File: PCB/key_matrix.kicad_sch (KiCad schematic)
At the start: 36 parts

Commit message: latest changes
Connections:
- net COL-3: now also MX116.1
- net COL-4: now also MX117.1
- net COL-5: now also MX118.1
- net ROW-1: no longer D116.1 (K)
- net ROW-2: no longer D117.1 (K)
- net ROW-3: no longer D118.1 (K)
- removed net COL-6: MX116.1, MX117.1, MX118.1
- new net ROW-4: D116.1 (K), D117.1 (K), D118.1 (K)
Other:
- moved on the sheet: D101, D102, D103, D104, D105, D106, D107, D108, D109, D110, D111, D112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

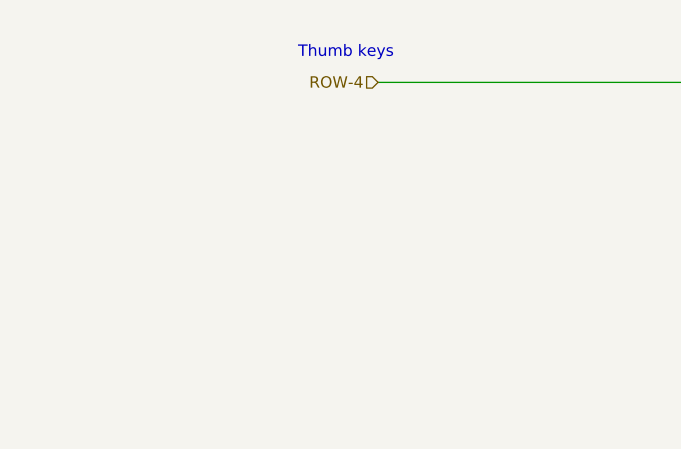
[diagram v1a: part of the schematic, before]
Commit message: Add mounting holes
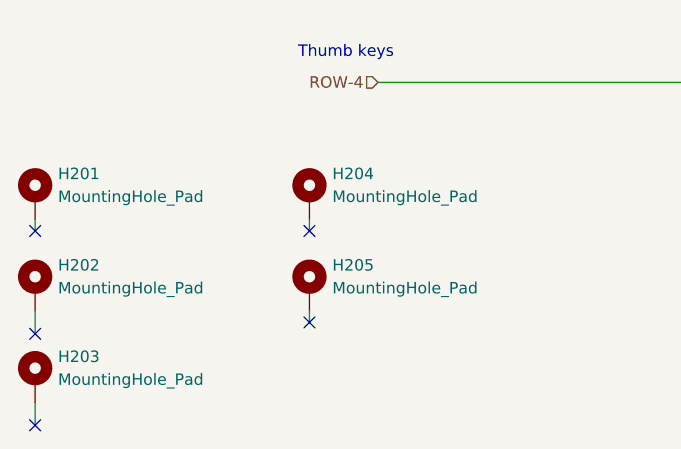
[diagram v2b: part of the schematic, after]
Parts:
- added H201, H202, H203, H204, H205: MountingHole_Pad, Footprints:M2_HOLE_v3, symbol Mechanical:MountingHole_Pad
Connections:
- no-connect marks 0 -> 5
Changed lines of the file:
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@@
   (junction (at 72.39 49.53) (diameter 0) (color 0 0 0 0)
   )
+  (no_connect (at 21.59 123.19))
+  (no_connect (at 21.59 133.35))
+  (no_connect (at 52.07 111.76))
+  (no_connect (at 52.07 121.92))
+  (no_connect (at 21.59 111.76))
   (wire (pts (xy 80.01 41.91) (xy 80.01 57.15))
     (stroke (width 0) (type default) (color 0 0 0 0))
@@
     (stroke (width 0) (type default) (color 0 0 0 0))
   )
+  (wire (pts (xy 52.07 110.49) (xy 52.07 111.76))
+    (stroke (width 0) (type default) (color 0 0 0 0))
+  )
   (wire (pts (xy 72.39 80.01) (xy 90.17 80.01))
     (stroke (width 0) (type default) (color 0 0 0 0))
   )
+  (wire (pts (xy 21.59 130.81) (xy 21.59 133.35))
+    (stroke (width 0) (type default) (color 0 0 0 0))
+  )
   (wire (pts (xy 125.73 95.25) (xy 143.51 95.25))
     (stroke (width 0) (type default) (color 0 0 0 0))
@@
     (stroke (width 0) (type default) (color 0 0 0 0))
   )
+  (wire (pts (xy 21.59 120.65) (xy 21.59 123.19))
+    (stroke (width 0) (type default) (color 0 0 0 0))
+  )
   (wire (pts (xy 97.79 33.02) (xy 97.79 41.91))
     (stroke (width 0) (type default) (color 0 0 0 0))
@@
     (stroke (width 0) (type default) (color 0 0 0 0))
   )
+  (wire (pts (xy 52.07 120.65) (xy 52.07 121.92))
+    (stroke (width 0) (type default) (color 0 0 0 0))
+  )
   (wire (pts (xy 115.57 72.39) (xy 115.57 87.63))
+    (stroke (width 0) (type default) (color 0 0 0 0))
+  )
+  (wire (pts (xy 21.59 111.76) (xy 21.59 110.49))
     (stroke (width 0) (type default) (color 0 0 0 0))
   )
@@
     (pin "2")
   )
+  (symbol (lib_id "Mechanical:MountingHole_Pad") (at 21.59 128.27 0) (unit 1)
+    (in_bom yes) (on_board yes) (fields_autoplaced)
+    (property "Reference" "H203" (id 0) (at 24.13 125.7299 0)
+      (effects (font (size 1.27 1.27)) (justify left))
+    )
+    (property "Value" "MountingHole_Pad" (id 1) (at 24.13 128.2699 0)
+      (effects (font (size 1.27 1.27)) (justify left))
+    )
+    (property "Footprint" "Footprints:M2_HOLE_v3" (id 2) (at 21.59 128.27 0)
+      (effects (font (size 1.27 1.27)) hide)
+    )
+    (property "Datasheet" "~" (id 3) (at 21.59 128.27 0)
+      (effects (font (size 1.27 1.27)) hide)
+    )
+    (pin "1")
+  )
   (symbol (lib_id "Switch:SW_Push") (at 102.87 87.63 0) (unit 1)
     (in_bom yes) (on_board yes)
@@
     (pin "2")
   )
+  (symbol (lib_id "Mechanical:MountingHole_Pad") (at 21.59 118.11 0) (unit 1)
+    (in_bom yes) (on_board yes) (fields_autoplaced)
+    (property "Reference" "H202" (id 0) (at 24.13 115.5699 0)
+      (effects (font (size 1.27 1.27)) (justify left))
+    )
+    (property "Value" "MountingHole_Pad" (id 1) (at 24.13 118.1099 0)
+      (effects (font (size 1.27 1.27)) (justify left))
+    )
+    (property "Footprint" "Footprints:M2_HOLE_v3" (id 2) (at 21.59 118.11 0)
+      (effects (font (size 1.27 1.27)) hide)
+    )
+    (property "Datasheet" "~" (id 3) (at 21.59 118.11 0)
+      (effects (font (size 1.27 1.27)) hide)
+    )
+    (pin "1")
+  )
   (symbol (lib_id "Diode:1N4148W") (at 125.73 60.96 270) (mirror x) (unit 1)
     (in_bom yes) (on_board yes)
@@
     (pin "2")
   )
+  (symbol (lib_id "Mechanical:MountingHole_Pad") (at 52.07 118.11 0) (unit 1)
+    (in_bom yes) (on_board yes) (fields_autoplaced)
+    (property "Reference" "H205" (id 0) (at 54.61 115.5699 0)
+      (effects (font (size 1.27 1.27)) (justify left))
+    )
+    (property "Value" "MountingHole_Pad" (id 1) (at 54.61 118.1099 0)
+      (effects (font (size 1.27 1.27)) (justify left))
+    )
+    (property "Footprint" "Footprints:M2_HOLE_v3" (id 2) (at 52.07 118.11 0)
+      (effects (font (size 1.27 1.27)) hide)
+    )
+    (property "Datasheet" "~" (id 3) (at 52.07 118.11 0)
+      (effects (font (size 1.27 1.27)) hide)
+    )
+    (pin "1")
+  )
   (symbol (lib_id "Diode:1N4148W") (at 90.17 76.2 90) (unit 1)
     (in_bom yes) (on_board yes)
@@
     (pin "2")
   )
+  (symbol (lib_id "Mechanical:MountingHole_Pad") (at 52.07 107.95 0) (unit 1)
+    (in_bom yes) (on_board yes) (fields_autoplaced)
+    (property "Reference" "H204" (id 0) (at 54.61 105.4099 0)
+      (effects (font (size 1.27 1.27)) (justify left))
+    )
+    (property "Value" "MountingHole_Pad" (id 1) (at 54.61 107.9499 0)
+      (effects (font (size 1.27 1.27)) (justify left))
+    )
+    (property "Footprint" "Footprints:M2_HOLE_v3" (id 2) (at 52.07 107.95 0)
+      (effects (font (size 1.27 1.27)) hide)
+    )
+    (property "Datasheet" "~" (id 3) (at 52.07 107.95 0)
+      (effects (font (size 1.27 1.27)) hide)
+    )
+    (pin "1")
+  )
   (symbol (lib_id "Diode:1N4148W") (at 107.95 60.96 270) (mirror x) (unit 1)
     (in_bom yes) (on_board yes)
@@
     (pin "2")
   )
+  (symbol (lib_id "Mechanical:MountingHole_Pad") (at 21.59 107.95 0) (unit 1)
+    (in_bom yes) (on_board yes) (fields_autoplaced)
+    (property "Reference" "H201" (id 0) (at 24.13 105.4099 0)
+      (effects (font (size 1.27 1.27)) (justify left))
+    )
+    (property "Value" "MountingHole_Pad" (id 1) (at 24.13 107.9499 0)
+      (effects (font (size 1.27 1.27)) (justify left))
+    )
+    (property "Footprint" "Footprints:M2_HOLE_v3" (id 2) (at 21.59 107.95 0)
+      (effects (font (size 1.27 1.27)) hide)
+    )
+    (property "Datasheet" "~" (id 3) (at 21.59 107.95 0)
+      (effects (font (size 1.27 1.27)) hide)
+    )
+    (pin "1")
+  )
   (symbol (lib_id "Diode:1N4148W") (at 72.39 76.2 270) (mirror x) (unit 1)

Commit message: Metric
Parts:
- renumbered H201 to H101, H202 to H102, H203 to H103, H204 to H104, H205 to H105
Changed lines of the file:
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@@
   (symbol (lib_id "Mechanical:MountingHole_Pad") (at 21.59 128.27 0) (unit 1)
     (in_bom yes) (on_board yes) (fields_autoplaced)
-    (property "Reference" "H203" (id 0) (at 24.13 125.7299 0)
+    (property "Reference" "H103" (id 0) (at 24.13 125.7299 0)
       (effects (font (size 1.27 1.27)) (justify left))
     )
@@
   (symbol (lib_id "Mechanical:MountingHole_Pad") (at 21.59 118.11 0) (unit 1)
     (in_bom yes) (on_board yes) (fields_autoplaced)
-    (property "Reference" "H202" (id 0) (at 24.13 115.5699 0)
+    (property "Reference" "H102" (id 0) (at 24.13 115.5699 0)
       (effects (font (size 1.27 1.27)) (justify left))
     )
@@
   (symbol (lib_id "Mechanical:MountingHole_Pad") (at 52.07 118.11 0) (unit 1)
     (in_bom yes) (on_board yes) (fields_autoplaced)
-    (property "Reference" "H205" (id 0) (at 54.61 115.5699 0)
+    (property "Reference" "H105" (id 0) (at 54.61 115.5699 0)
       (effects (font (size 1.27 1.27)) (justify left))
     )
@@
   (symbol (lib_id "Mechanical:MountingHole_Pad") (at 52.07 107.95 0) (unit 1)
     (in_bom yes) (on_board yes) (fields_autoplaced)
-    (property "Reference" "H204" (id 0) (at 54.61 105.4099 0)
+    (property "Reference" "H104" (id 0) (at 54.61 105.4099 0)
       (effects (font (size 1.27 1.27)) (justify left))
     )
@@
   (symbol (lib_id "Mechanical:MountingHole_Pad") (at 21.59 107.95 0) (unit 1)
     (in_bom yes) (on_board yes) (fields_autoplaced)
-    (property "Reference" "H201" (id 0) (at 24.13 105.4099 0)
-      (effects (font (size 1.27 1.27)) (justify left))
-    )
+    (property "Reference" "H101" (id 0) (at 24.13 105.4099 0)
+      (effects (font (size 1.27 1.27)) (justify left))
+    )
